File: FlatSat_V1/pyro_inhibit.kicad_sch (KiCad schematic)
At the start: 20 parts, among them SW600 MSK12C02

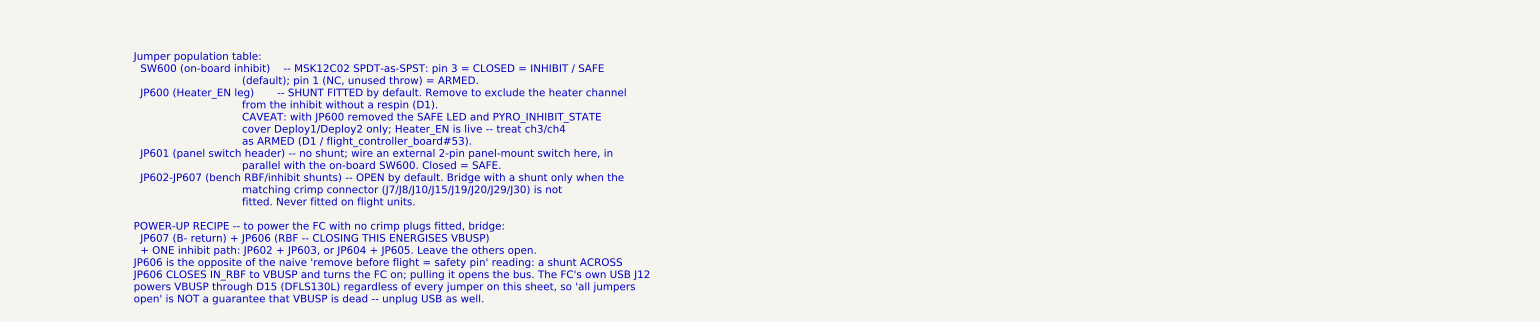
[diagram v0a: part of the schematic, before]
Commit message: FlatSat V1: apply review pass 2 fix-this-rev items 1-3
1 J510 moved to (262.0,168.93): shell face 0.46 mm proud of the edge per
  the HRO drawing (was 2.41 mm recessed); escapes stretched, no new copper.
2 J500 over-voltage block on the battery sheet (OVP <= 9 V, trip check,
  never the VSOLAR supply) and 8.4V MAX silk.
3 Gate-drive probing note (TP501-TP504 reference floating nets) on the
  sheet and in the review ATP text. Item 6 Mode 2 ISS-bypass note added.

Gates: heritage refill 0, attachment 0/7/37, DRC 14/1/11 (item set
unchanged), via-in-pad 0/0, track_width 95, ERC 12.

Co-Authored-By: Claude Opus 5.5 (1M context) <noreply@anthropic.com>
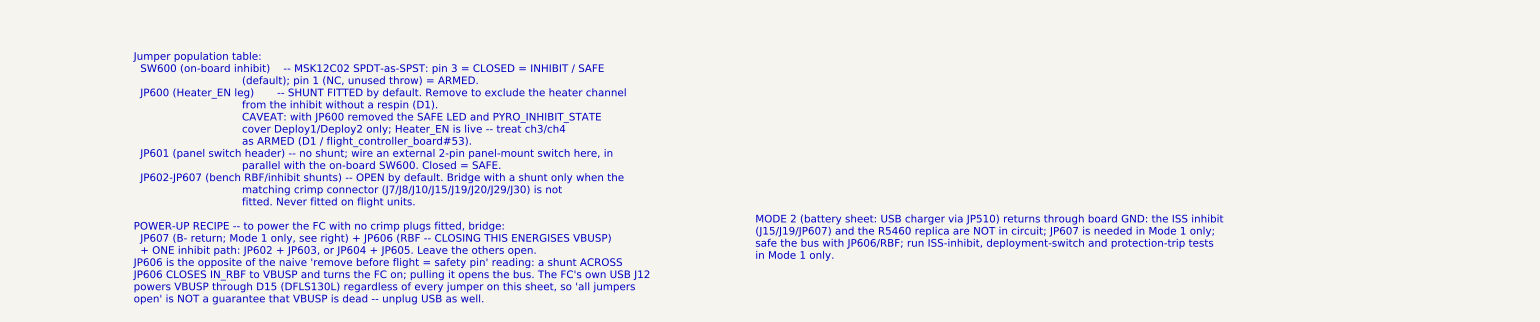
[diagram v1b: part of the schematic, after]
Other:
- note added: "MODE 2 (battery sheet: USB charger via JP510) returns through board GND: the ISS inhibit (J15/J19/JP607) and the R5460 replica are NOT in circuit; JP607 is needed in Mode 1 only; safe the bus with JP606/RBF; run ISS-inhibit, deployment-switch and protection-trip tests in Mode 1 only."
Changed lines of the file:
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@@
+		)
+	)
+	(text "MODE 2 (battery sheet: USB charger via JP510) returns through board GND: the ISS inhibit\n(J15/J19/JP607) and the R5460 replica are NOT in circuit; JP607 is needed in Mode 1 only;\nsafe the bus with JP606/RBF; run ISS-inhibit, deployment-switch and protection-trip tests\nin Mode 1 only."
+		(exclude_from_sim no)
+		(at 107.95 265.43 0)
+		(effects
+			(font
+				(size 1.0 1.0)
+			)
+			(justify left top)
 		)
 	)
@@
 		)
 	)
-	(text "Jumper population table:\n  SW600 (on-board inhibit)    -- MSK12C02 SPDT-as-SPST: pin 3 = CLOSED = INHIBIT / SAFE\n                                 (default); pin 1 (NC, unused throw) = ARMED.\n  JP600 (Heater_EN leg)       -- SHUNT FITTED by default. Remove to exclude the heater channel\n                                 from the inhibit without a respin (D1).\n                                 CAVEAT: with JP600 removed the SAFE LED and PYRO_INHIBIT_STATE\n                                 cover Deploy1/Deploy2 only; Heater_EN is live -- treat ch3/ch4\n                                 as ARMED (D1 / flight_controller_board#53).\n  JP601 (panel switch header) -- no shunt; wire an external 2-pin panel-mount switch here, in\n                                 parallel with the on-board SW600. Closed = SAFE.\n  JP602-JP607 (bench RBF/inhibit shunts) -- OPEN by default. Bridge with a shunt only when the\n                                 matching crimp connector (J7/J8/J10/J15/J19/J20/J29/J30) is not\n                                 fitted. Never fitted on flight units.\n\nPOWER-UP RECIPE -- to power the FC with no crimp plugs fitted, bridge:\n  JP607 (B- return) + JP606 (RBF -- CLOSING THIS ENERGISES VBUSP)\n  + ONE inhibit path: JP602 + JP603, or JP604 + JP605. Leave the others open.\nJP606 is the opposite of the naive 'remove before flight = safety pin' reading: a shunt ACROSS\nJP606 CLOSES IN_RBF to VBUSP and turns the FC on; pulling it opens the bus. The FC's own USB J12\npowers VBUSP through D15 (DFLS130L) regardless of every jumper on this sheet, so 'all jumpers\nopen' is NOT a guarantee that VBUSP is dead -- unplug USB as well."
+	(text "Jumper population table:\n  SW600 (on-board inhibit)    -- MSK12C02 SPDT-as-SPST: pin 3 = CLOSED = INHIBIT / SAFE\n                                 (default); pin 1 (NC, unused throw) = ARMED.\n  JP600 (Heater_EN leg)       -- SHUNT FITTED by default. Remove to exclude the heater channel\n                                 from the inhibit without a respin (D1).\n                                 CAVEAT: with JP600 removed the SAFE LED and PYRO_INHIBIT_STATE\n                                 cover Deploy1/Deploy2 only; Heater_EN is live -- treat ch3/ch4\n                                 as ARMED (D1 / flight_controller_board#53).\n  JP601 (panel switch header) -- no shunt; wire an external 2-pin panel-mount switch here, in\n                                 parallel with the on-board SW600. Closed = SAFE.\n  JP602-JP607 (bench RBF/inhibit shunts) -- OPEN by default. Bridge with a shunt only when the\n                                 matching crimp connector (J7/J8/J10/J15/J19/J20/J29/J30) is not\n                                 fitted. Never fitted on flight units.\n\nPOWER-UP RECIPE -- to power the FC with no crimp plugs fitted, bridge:\n  JP607 (B- return; Mode 1 only, see right) + JP606 (RBF -- CLOSING THIS ENERGISES VBUSP)\n  + ONE inhibit path: JP602 + JP603, or JP604 + JP605. Leave the others open.\nJP606 is the opposite of the naive 'remove before flight = safety pin' reading: a shunt ACROSS\nJP606 CLOSES IN_RBF to VBUSP and turns the FC on; pulling it opens the bus. The FC's own USB J12\npowers VBUSP through D15 (DFLS130L) regardless of every jumper on this sheet, so 'all jumpers\nopen' is NOT a guarantee that VBUSP is dead -- unplug USB as well."
 		(exclude_from_sim no)
 		(at 25.4 243.84 0)

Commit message: FlatSat V1: fix 8 wrong-part LCSC fields; header collapse; sync project.db
35 Phase-1/2 footprints carried a stale board-only LCSC field cloned
from heritage footprints; the JLC plugin reads it before LCSC Part, so
8 would have been ordered wrong: C221/C222 (15 pF) and C301 (10 nF) and
C304 (1 uF) as C1525 100 nF; D201/D202/D510/LED600 as C12624. Removed
the stale field from all 35 (fields only, no geometry).

PLM-08: the 13 identical 1x02 headers now all use C492401. U1 LCSC field
-> C181596 (TSSOP, matches project.db and Rev2).

project.db synced with JLCPCB Tools release 2026.04.03's own Store code
(owner request 2026-10-22): 258 -> 481 rows, 223 added, 0 changed.

Gates unchanged: heritage refill 0, attachment 0/7/37, DRC 14/1/11,
via-in-pad 0/0, ERC 12.

Co-Authored-By: Claude Opus 5.5 (1M context) <noreply@anthropic.com>
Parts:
- JP600, JP601, JP602, JP603, JP604, JP605, JP606, JP607: LCSC Part C124375 -> C492401
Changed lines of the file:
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@@
 			)
 		)
-		(property "Datasheet" "https://www.lcsc.com/datasheet/lcsc_datasheet_2411220201_Ckmtw-Shenzhen-Cankemeng-B-2100S02P-A110_C124375.pdf"
+		(property "Datasheet" "https://www.lcsc.com/datasheet/lcsc_datasheet_2409302300_XFCN-PZ254V-11-02P_C492401.pdf"
 			(at 40.64 57.15 0)
 			(hide yes)
@@
 			)
 		)
-		(property "LCSC Part" "C124375"
+		(property "LCSC Part" "C492401"
 			(at 40.64 57.15 0)
 			(hide yes)
@@
 			)
 		)
-		(property "Datasheet" "https://www.lcsc.com/datasheet/lcsc_datasheet_2411220201_Ckmtw-Shenzhen-Cankemeng-B-2100S02P-A110_C124375.pdf"
+		(property "Datasheet" "https://www.lcsc.com/datasheet/lcsc_datasheet_2409302300_XFCN-PZ254V-11-02P_C492401.pdf"
 			(at 81.28 107.95 0)
 			(hide yes)
@@
 			)
 		)
-		(property "LCSC Part" "C124375"
+		(property "LCSC Part" "C492401"
 			(at 81.28 107.95 0)
 			(hide yes)
@@
 			)
 		)
-		(property "Datasheet" "https://www.lcsc.com/datasheet/lcsc_datasheet_2411220201_Ckmtw-Shenzhen-Cankemeng-B-2100S02P-A110_C124375.pdf"
+		(property "Datasheet" "https://www.lcsc.com/datasheet/lcsc_datasheet_2409302300_XFCN-PZ254V-11-02P_C492401.pdf"
 			(at 58.42 154.94 0)
 			(hide yes)
@@
 			)
 		)
-		(property "LCSC Part" "C124375"
+		(property "LCSC Part" "C492401"
 			(at 58.42 154.94 0)
 			(hide yes)
@@
 			)
 		)
-		(property "Datasheet" "https://www.lcsc.com/datasheet/lcsc_datasheet_2411220201_Ckmtw-Shenzhen-Cankemeng-B-2100S02P-A110_C124375.pdf"
+		(property "Datasheet" "https://www.lcsc.com/datasheet/lcsc_datasheet_2409302300_XFCN-PZ254V-11-02P_C492401.pdf"
 			(at 58.42 170.18 0)
 			(hide yes)
@@
 			)
 		)
-		(property "LCSC Part" "C124375"
+		(property "LCSC Part" "C492401"
 			(at 58.42 170.18 0)
 			(hide yes)
@@
 			)
 		)
-		(property "Datasheet" "https://www.lcsc.com/datasheet/lcsc_datasheet_2411220201_Ckmtw-Shenzhen-Cankemeng-B-2100S02P-A110_C124375.pdf"
+		(property "Datasheet" "https://www.lcsc.com/datasheet/lcsc_datasheet_2409302300_XFCN-PZ254V-11-02P_C492401.pdf"
 			(at 58.42 185.42 0)
 			(hide yes)
@@
 			)
 		)
-		(property "LCSC Part" "C124375"
+		(property "LCSC Part" "C492401"
 			(at 58.42 185.42 0)
 			(hide yes)
@@
 			)
 		)
-		(property "Datasheet" "https://www.lcsc.com/datasheet/lcsc_datasheet_2411220201_Ckmtw-Shenzhen-Cankemeng-B-2100S02P-A110_C124375.pdf"
+		(property "Datasheet" "https://www.lcsc.com/datasheet/lcsc_datasheet_2409302300_XFCN-PZ254V-11-02P_C492401.pdf"
 			(at 58.42 200.66 0)
 			(hide yes)
@@
 			)
 		)
-		(property "LCSC Part" "C124375"
+		(property "LCSC Part" "C492401"
 			(at 58.42 200.66 0)
 			(hide yes)
@@
 			)
 		)
-		(property "Datasheet" "https://www.lcsc.com/datasheet/lcsc_datasheet_2411220201_Ckmtw-Shenzhen-Cankemeng-B-2100S02P-A110_C124375.pdf"
+		(property "Datasheet" "https://www.lcsc.com/datasheet/lcsc_datasheet_2409302300_XFCN-PZ254V-11-02P_C492401.pdf"
 			(at 58.42 215.9 0)
 			(hide yes)
@@
 			)
 		)
-		(property "LCSC Part" "C124375"
+		(property "LCSC Part" "C492401"
 			(at 58.42 215.9 0)
 			(hide yes)
@@
 			)
 		)
-		(property "Datasheet" "https://www.lcsc.com/datasheet/lcsc_datasheet_2411220201_Ckmtw-Shenzhen-Cankemeng-B-2100S02P-A110_C124375.pdf"
+		(property "Datasheet" "https://www.lcsc.com/datasheet/lcsc_datasheet_2409302300_XFCN-PZ254V-11-02P_C492401.pdf"
 			(at 58.42 231.14 0)
 			(hide yes)
@@
 			)
 		)
-		(property "LCSC Part" "C124375"
+		(property "LCSC Part" "C492401"
 			(at 58.42 231.14 0)
 			(hide yes)
